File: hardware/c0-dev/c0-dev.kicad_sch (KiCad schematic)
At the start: 0 parts

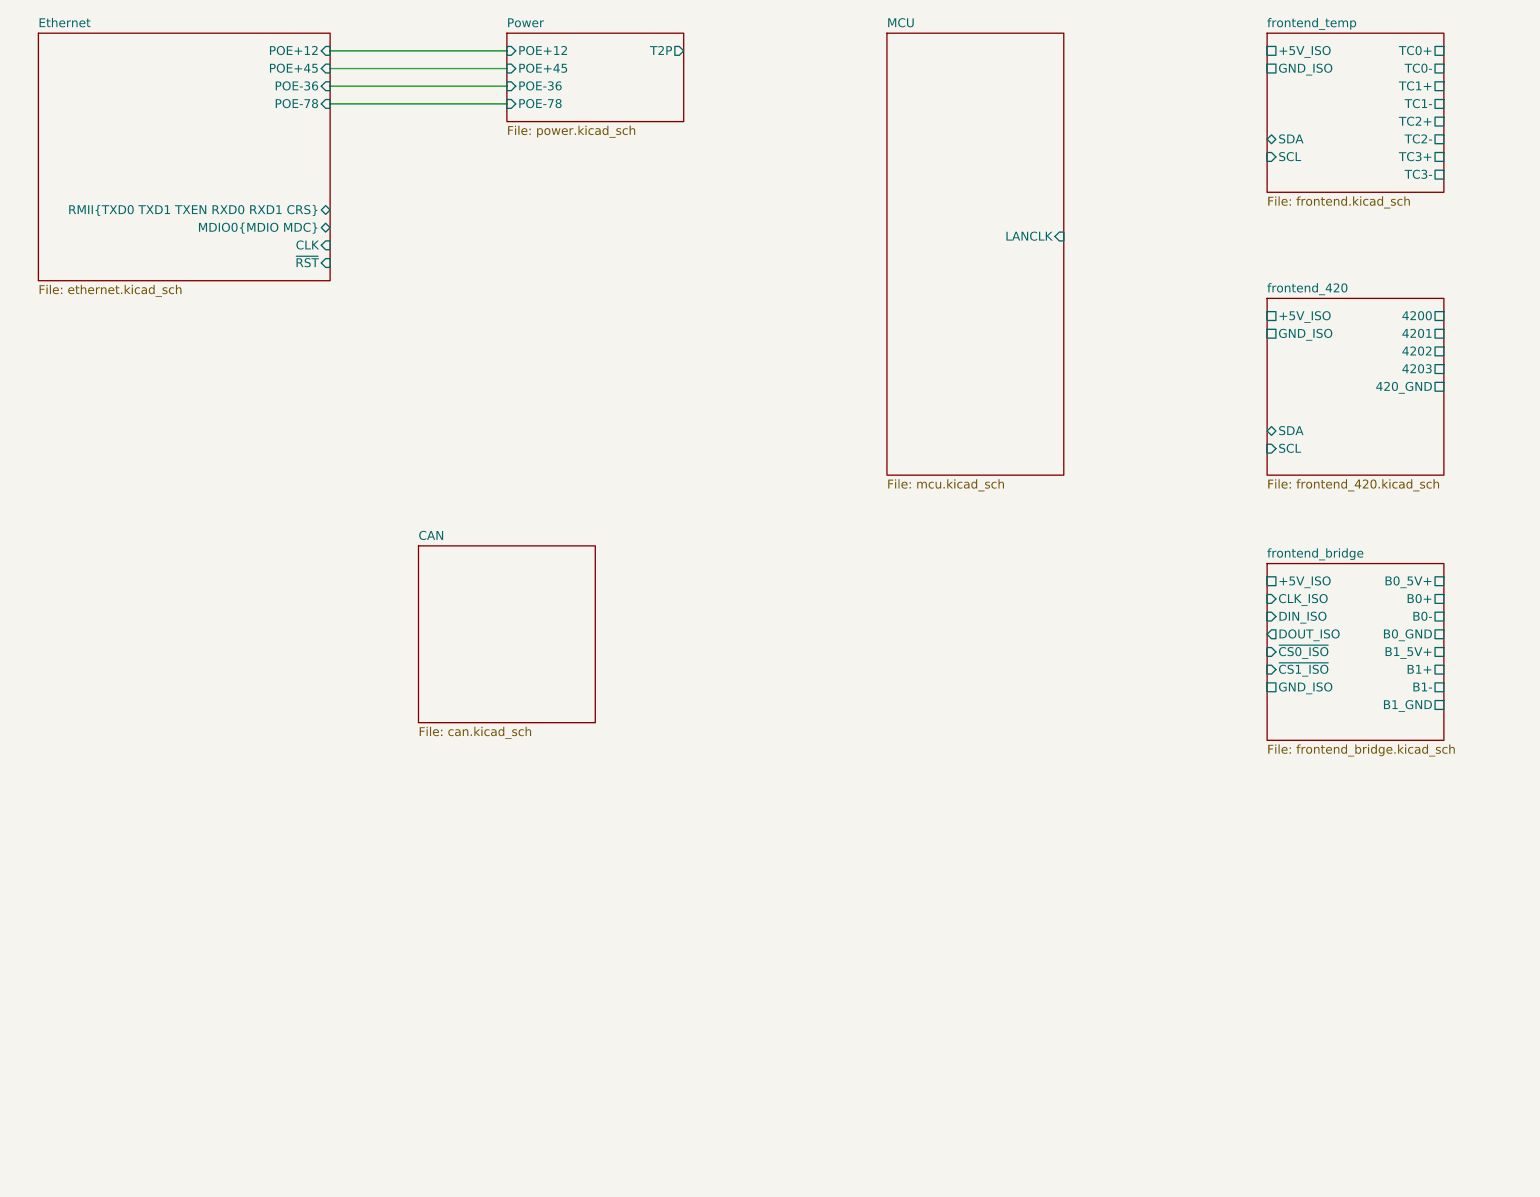
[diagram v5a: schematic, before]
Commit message: 3.3V logic level + digital inputs
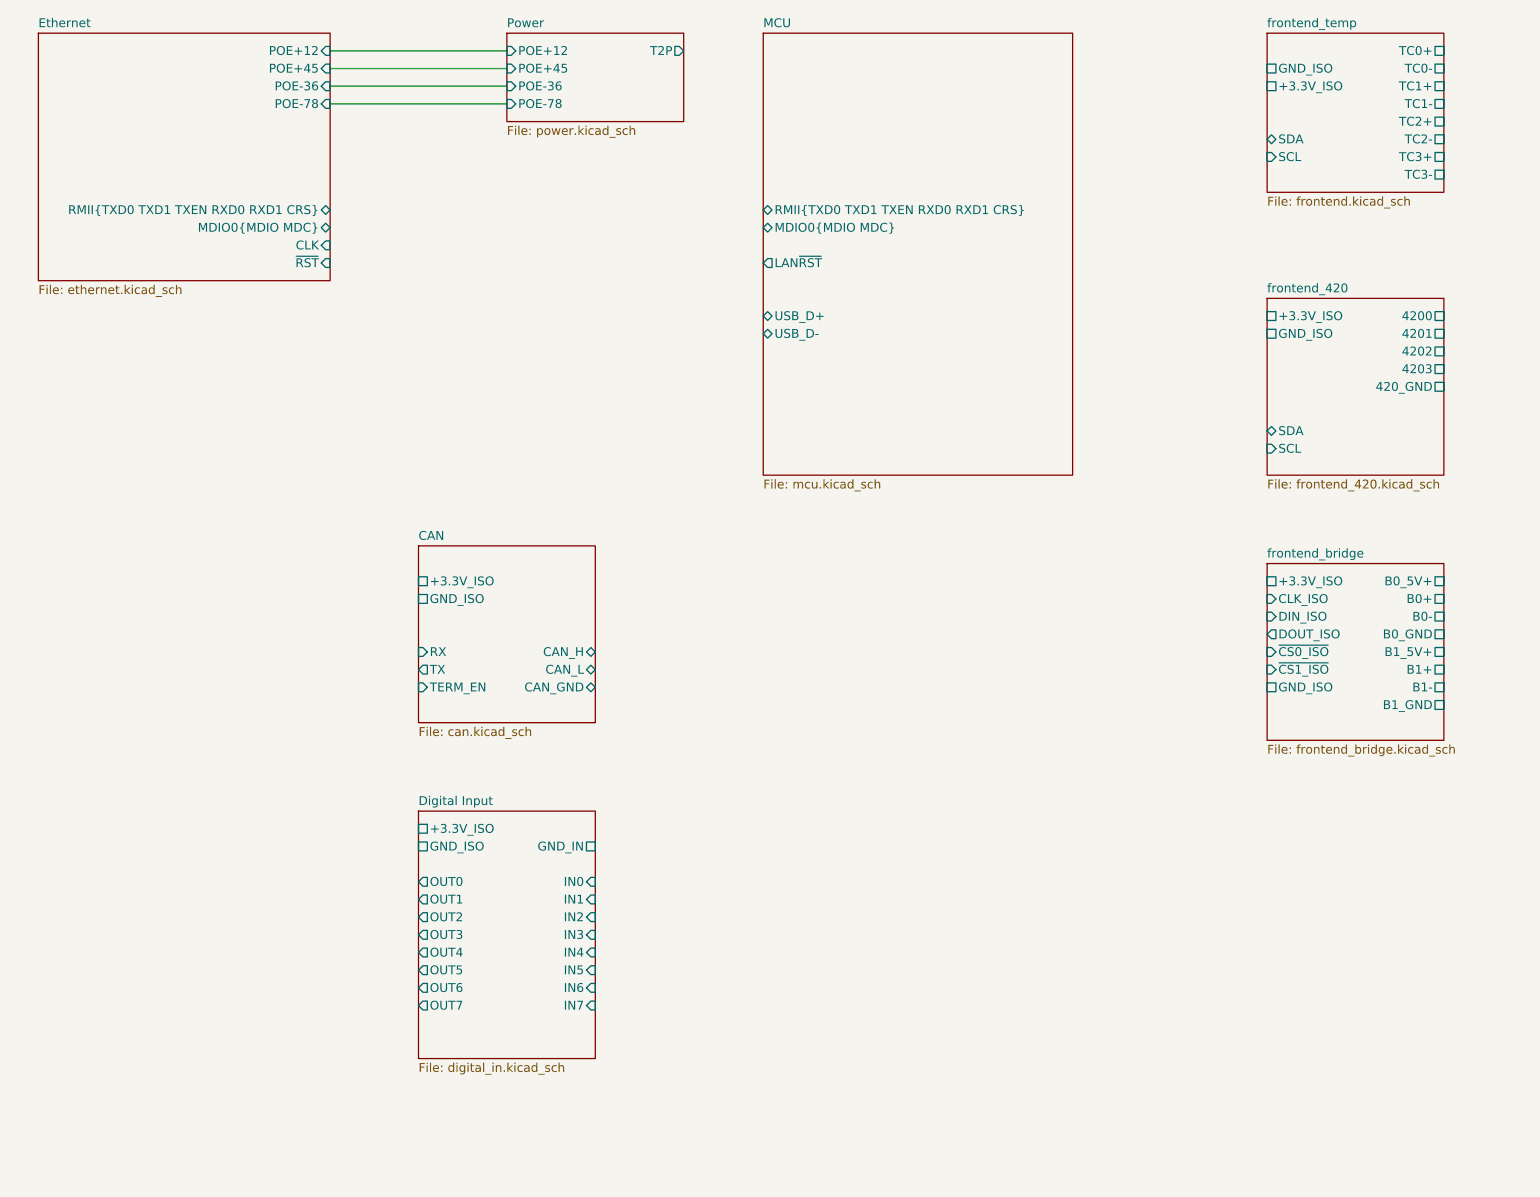
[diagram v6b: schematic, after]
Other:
- added sheet Digital Input (digital_in.kicad_sch)
- sheet CAN ports: added +3.3V_ISO, CAN_GND, CAN_H, CAN_L, GND_ISO, RX, TERM_EN, TX; removed none
- sheet MCU ports: added LAN~{RST}, MDIO0{MDIO MDC}, RMII{TXD0 TXD1 TXEN RXD0 RXD1 CRS}, USB_D+, USB_D-; removed LANCLK
- sheet frontend_420 ports: added +3.3V_ISO; removed +5V_ISO
- sheet frontend_bridge ports: added +3.3V_ISO; removed +5V_ISO
- sheet frontend_temp ports: added +3.3V_ISO; removed +5V_ISO

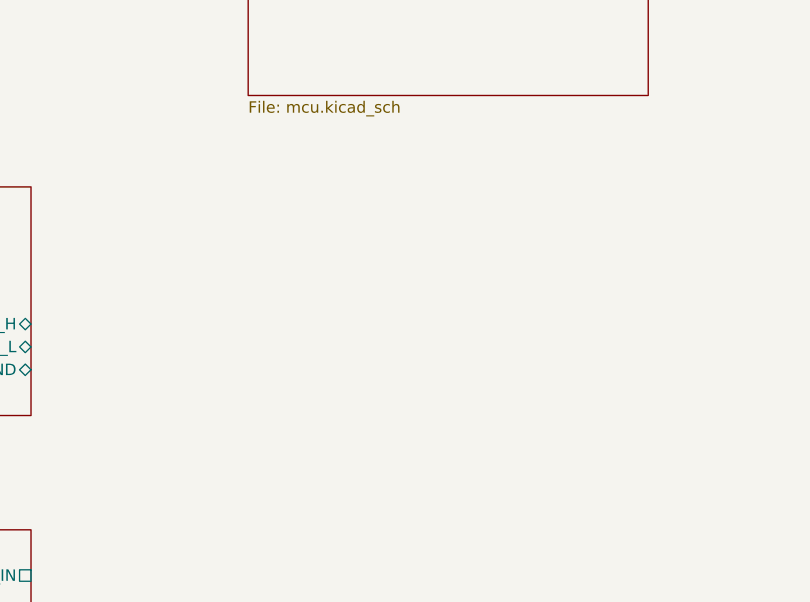
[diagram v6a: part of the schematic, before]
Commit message: efuse based DO
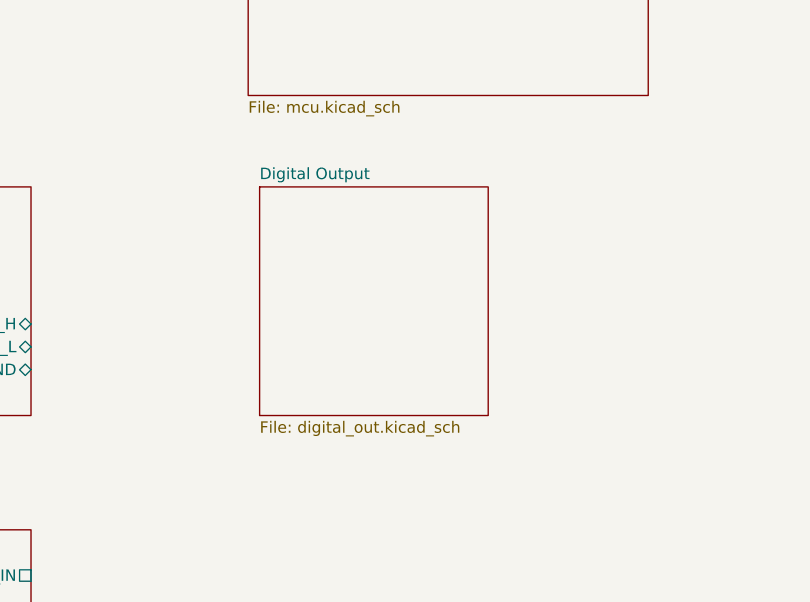
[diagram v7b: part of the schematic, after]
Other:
- added sheet Digital Output (digital_out.kicad_sch)
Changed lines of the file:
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@@
+	)
+	(sheet
+		(at 127 101.6)
+		(size 25.4 25.4)
+		(exclude_from_sim no)
+		(in_bom yes)
+		(on_board yes)
+		(dnp no)
+		(fields_autoplaced yes)
+		(stroke
+			(width 0.1524)
+			(type solid)
+		)
+		(fill
+			(color 0 0 0 0)
+		)
+		(property "Sheetname" "Digital Output"
+			(at 127 100.8884 0)
+			(show_name no)
+			(do_not_autoplace no)
+			(effects
+				(font
+					(size 1.27 1.27)
+				)
+				(justify left bottom)
+			)
+		)
+		(property "Sheetfile" "digital_out.kicad_sch"
+			(at 127 127.5846 0)
+			(show_name no)
+			(do_not_autoplace no)
+			(effects
+				(font
+					(size 1.27 1.27)
+				)
+				(justify left top)
+			)
+		)
+		(instances
+			(project "c0-dev"
+				(path "/b8347a0e-ad04-4414-969d-3c64a611d74e"
+					(page "10")
+				)
+			)
+		)
 	)
 	(sheet

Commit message: i2c address check
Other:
- added sheet screen (screen.kicad_sch)
- sheet Digital Output ports: added +3.3V_ISO, 24V, GND_ISO, OUT0, OUT1, OUT2, OUT3, OUT4, OUT5, OUT6, OUT7, SCL, SDA; removed none
- sheet MCU ports: added I2C0{SDA SCL}, LAN_CLK; removed USB_D+, USB_D-
